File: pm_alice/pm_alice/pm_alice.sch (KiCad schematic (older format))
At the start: 197 parts, among them M1 MX-LED, M2 MX-LED, SW1 reset_button

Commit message: Fix annotations (pm alice)
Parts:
- renumbered d49 to r49
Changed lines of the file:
@@
 Connection ~ 5050 1550
 $Comp
-L Device:R_Small d49
+L Device:R_Small r49
 U 1 1 60034B02
 P 6350 1350
-F 0 "d49" H 6409 1396 50  0000 L CNN
+F 0 "r49" H 6409 1396 50  0000 L CNN
 F 1 "4.7k" H 6409 1305 50  0000 L CNN
 F 2 "Keebio-Parts:Resistor-Hybrid" H 6350 1350 50  0001 C CNN

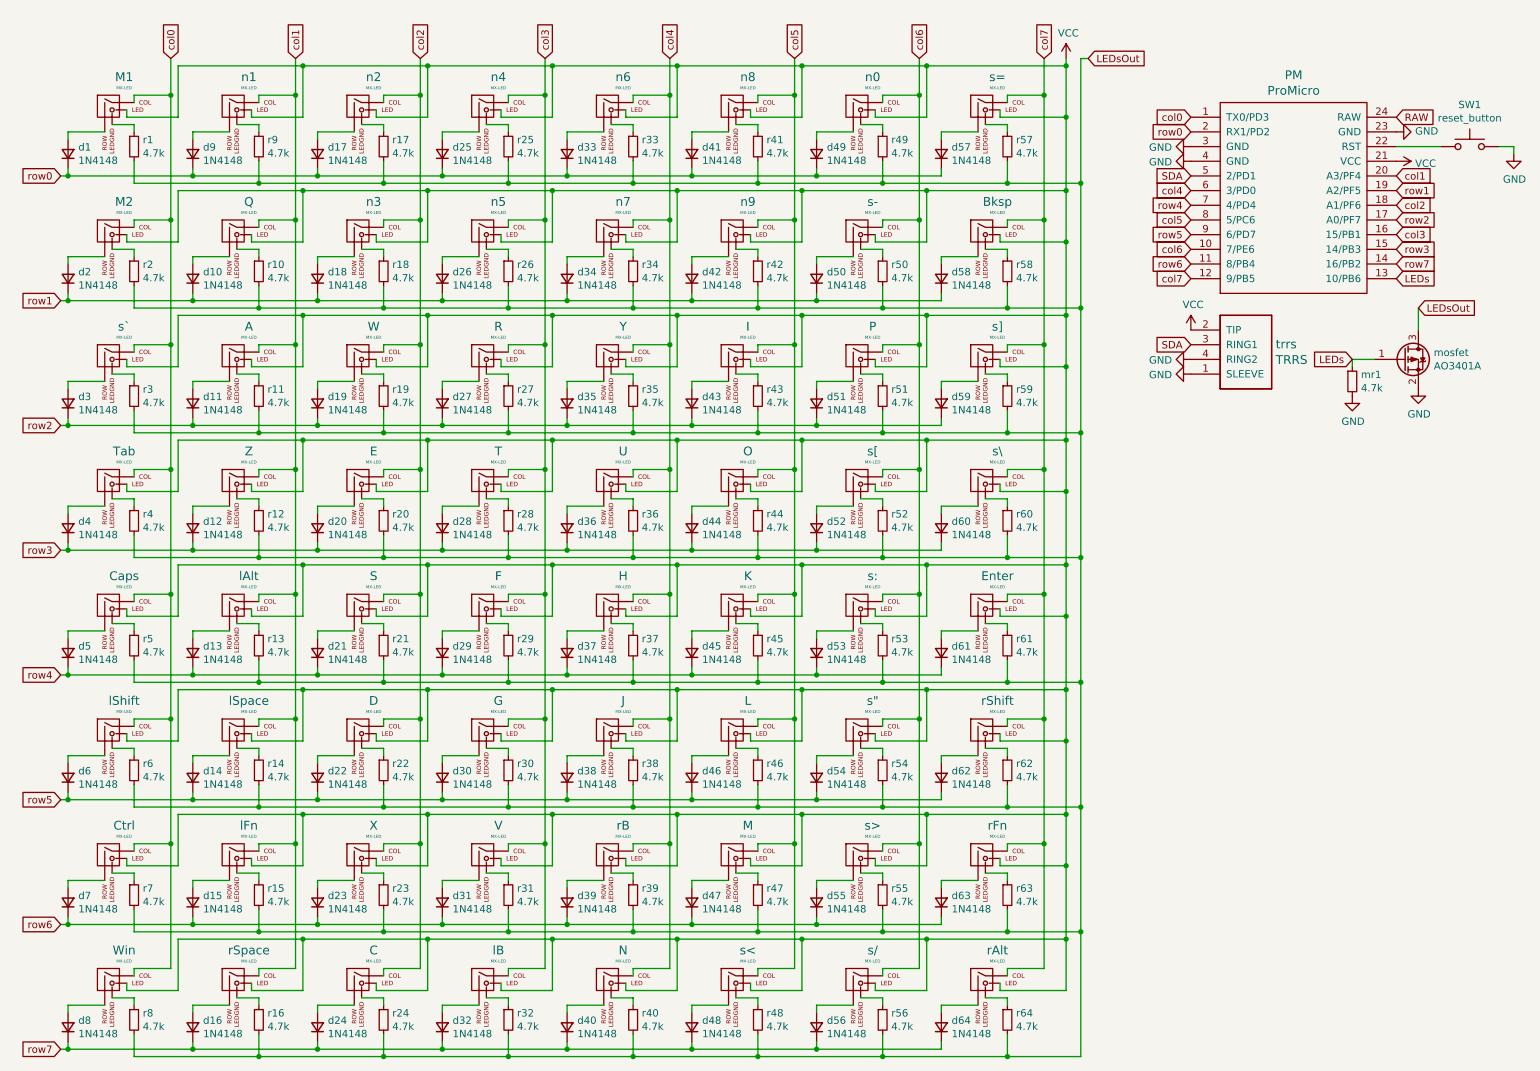
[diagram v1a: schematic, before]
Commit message: Kicad annotation for pm alice schematic
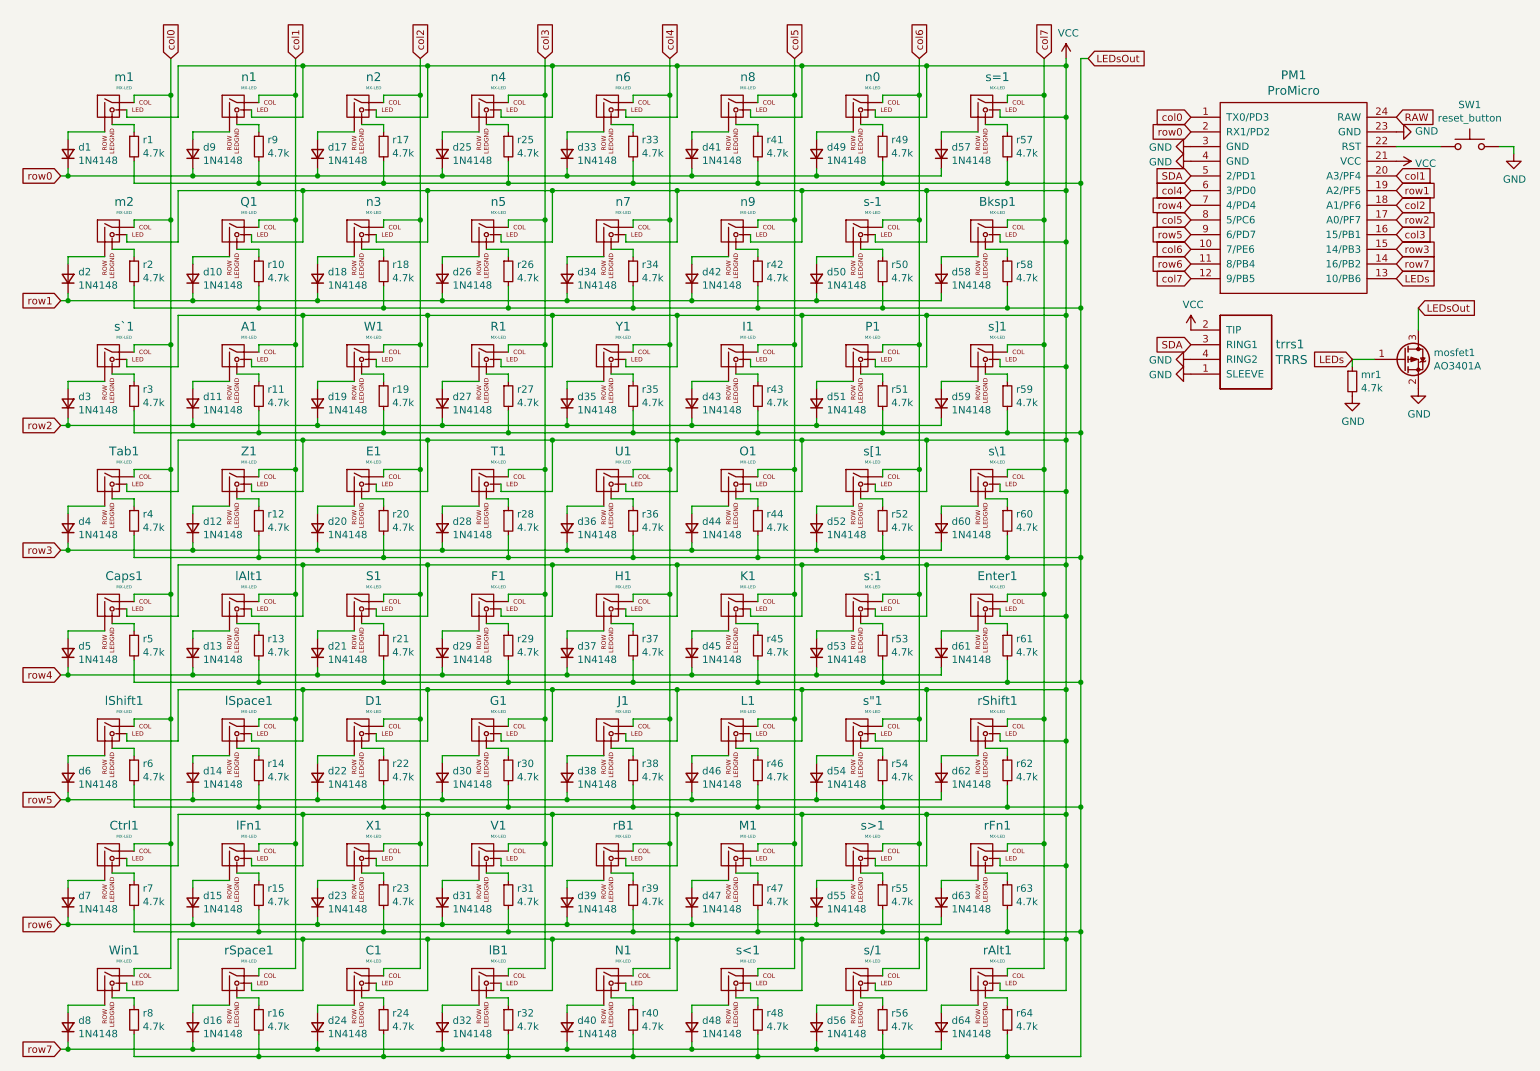
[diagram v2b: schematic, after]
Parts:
- rShift1: renamed from rShift; footprint Keebio-Parts:MX-Alps-Choc-2U -> Keebio-Parts:MX-Alps-Choc-1U
- renumbered A to A1, Bksp to Bksp1, C to C1, Caps to Caps1, Ctrl to Ctrl1, D to D1, E to E1, Enter to Enter1, F to F1, G to G1, H to H1, I to I1, J to J1, K to K1, L to L1, M to M1, N to N1, O to O1, P to P1, PM to PM1, Q to Q1, R to R1, S to S1, T to T1, Tab to Tab1, U to U1, V to V1, W to W1, Win to Win1, X to X1, Y to Y1, Z to Z1, lAlt to lAlt1, lB to lB1, lFn to lFn1, lShift to lShift1, lSpace to lSpace1, M1 to m1, M2 to m2, mosfet to mosfet1, rAlt to rAlt1, rB to rB1, rFn to rFn1, rSpace to rSpace1, s" to s"1, s- to s-1, s/ to s/1, s: to s:1, s< to s<1, s= to s=1, s> to s>1, s[ to s[1, s\ to s\1, s] to s]1, s` to s`1, trrs to trrs1
